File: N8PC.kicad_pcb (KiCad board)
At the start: 4 copper layers, 244 x 244 mm, 226 parts, among them J1 IRQ Selection, J10 Bus_ISA_8bit, J11 F18A TANG NANO Connector, J12 FRONT_PANEL, J13 IRQ Selection, J14 Bus_ISA_8bit, J15 MOUSE, J16 KEYBOARD, J17 TTL SERIAL CONSOLE, J18 TTL CONSOLE PWR, J19 TTL SERIAL CONSOLE, J2 IRQ Selection, J20 TTL CONSOLE PWR, J21 KEYBOARD IRQ, J22 BUS IRQ, J23 VIDEO IRQ, J3 Bus_ISA_8bit, J4 Bus_ISA_8bit, J5 IRQ Selection, J6 Bus_ISA_8bit, J7 IRQ Selection, J8 Bus_ISA_8bit, J9 IRQ Selection, K16 CONN_3, K17 CPU_CLK, K18 CONN_3, K2 IDE_PWR, K3 CONN_3, K4 CONN_3, K5 CONN_3, P1 IO_ADDR, P10 CONN_1, P11 CONN_10X2, P12 POWER_SW, P13 SERIAL, P14 14.31818 MHz CLK, P15 AUDIO, P16 IO_ADDR2, P18 SERIAL, P19 ASCI OSC, P2 CONN_1, P21 CONN_1, P22 CONN_1, P23 CONN_1, P27 FLOPPY, P29 PPIDE, P3 CONN_1, P31 PARALLEL EXP, P37 CPU OSC, P4 CONN_1, P41 OSC_FDC, P43 CHAN_MIX, P5 CONN_1, P51 JOYSTICK0, P52 JOYSTICK1, P6 CONN_1, P7 CONN_1, P8 CONN_1, P9 CONN_1, SW1 POWER, SW2 RESET, U1 74LS244, U10 MAX232, U12 74LS74, U13 27C080, U14 74LS125, U15 74LS245, U16 74LS244, U18 74LS32, U19 74HCT14, U2 74LS14, U21 74LS682N, U23 TMS9918 EMU, U24 CLK, U25 82c42, U26 74LS06, U29 DS1233, U3 74LS244, U31 74LS244, U32 74LS139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

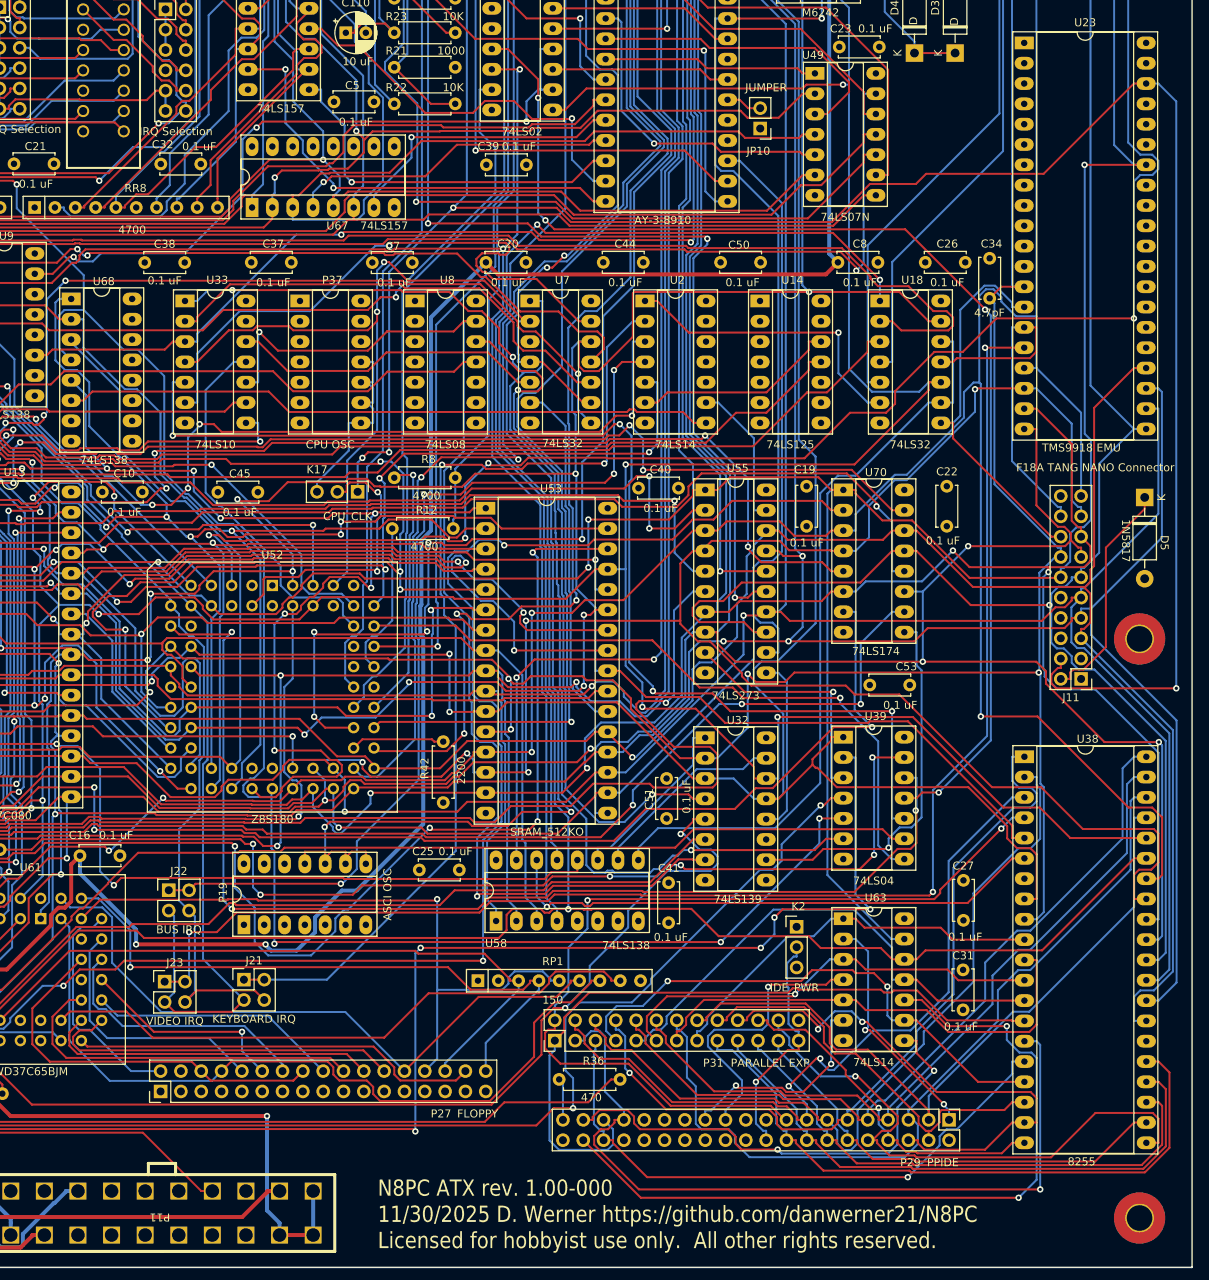
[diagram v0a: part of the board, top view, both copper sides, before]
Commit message: V1.1 PCB and schematic fix issue with data direction for bus
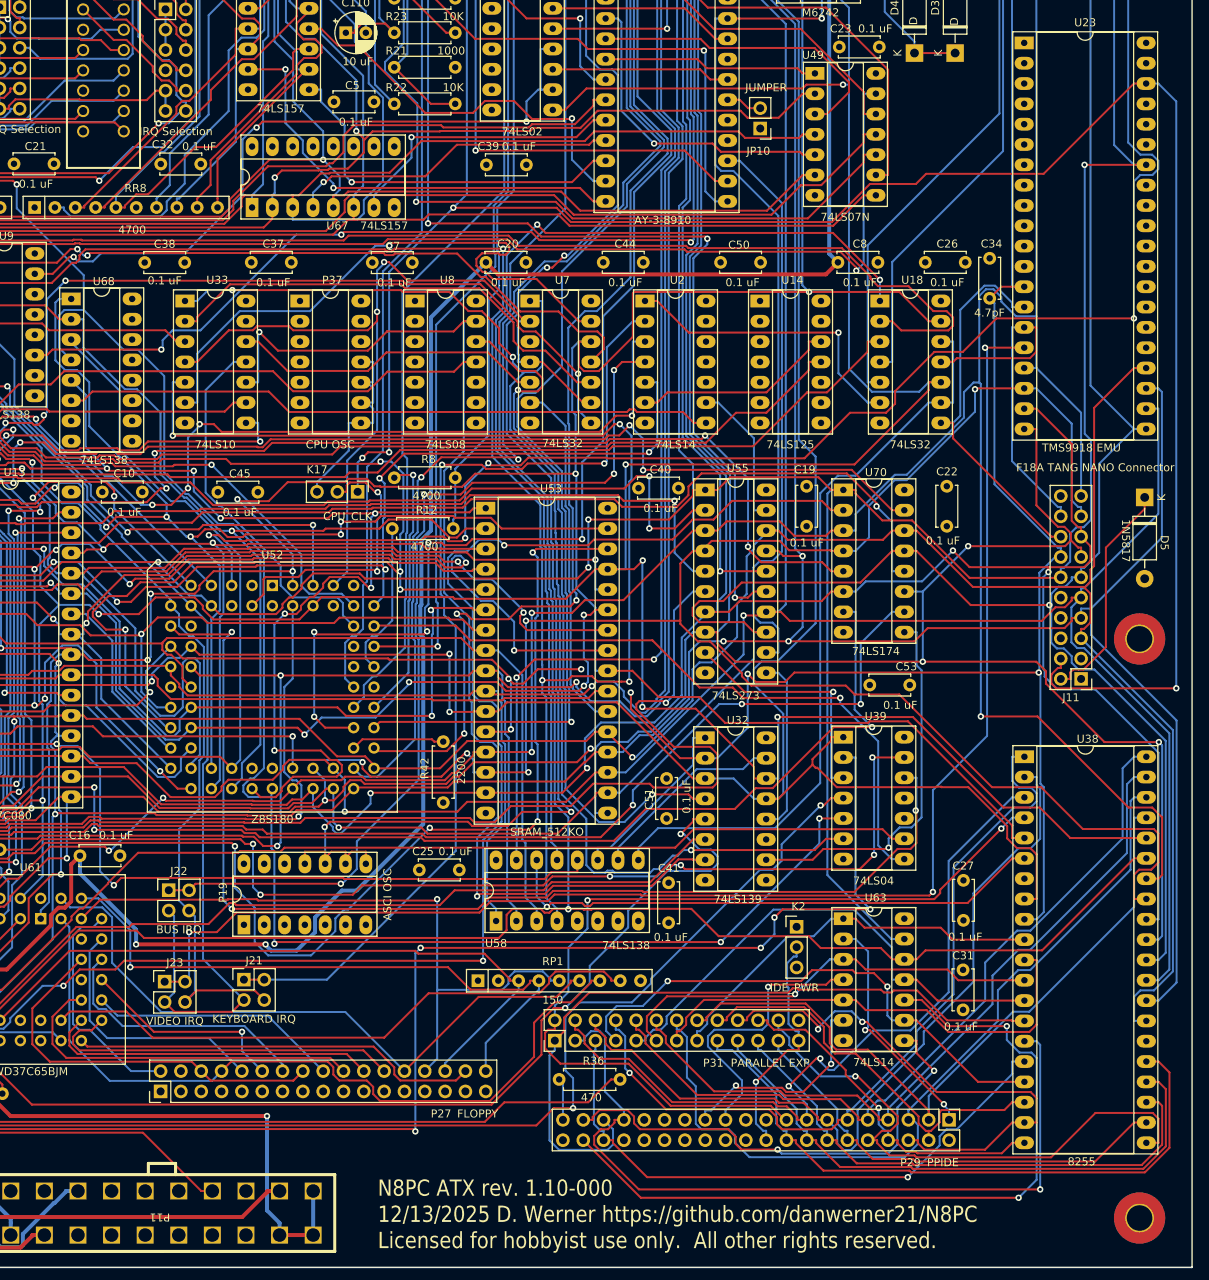
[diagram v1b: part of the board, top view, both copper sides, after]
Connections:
- U33 pad 3: /CS_RTC -> /INTIORQ2
- U33 pad 5: /INTIORQ -> /INTIORQ1
- U39 pad 10: /INTIORQ -> unconnected-(U39-Pad10)
- U39 pad 11: Net-(U39-Pad11) -> unconnected-(U39-Pad11)
- U5 pad 4: Net-(U39-Pad11) -> unconnected-(U5-Pad4)
- U5 pad 5: /INTIORQ1 -> unconnected-(U5-Pad5)
- U5 pad 6: /INTIORQ2 -> unconnected-(U5-Pad6)
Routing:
- net Net-(U39-Pad11): track 152.9 -> 0.00 mm, vias 4 -> 0
- net /INTIORQ: track 145.8 -> 0.00 mm, vias 4 -> 0
- net /INTIORQ1: track 213.8 -> 296.0 mm, vias 4 -> 7
- net /INTIORQ2: track 96.7 -> 36.6 mm, vias 1 -> 0
- net /WR: track 575.1 -> 580.2 mm, vias 7 -> 8
- net A0: track 559.8 -> 561.0 mm, vias 8 -> 10
- net /CS_RTC: vias 3 -> 4
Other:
- board text added: "N8PC ATX rev. 1.10-000 12/13/2025 D. Werner https://github.com/danwerner21/N8PC Licensed for hobbyist use only. All other rights reserved."
- board text removed: "N8PC ATX rev. 1.00-000 11/30/2025 D. Werner https://github.com/danwerner21/N8PC Licensed for hobbyist use only. All other rights reserved."
